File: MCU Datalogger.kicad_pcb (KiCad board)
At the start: 2 copper layers, 29 parts, among them J1 Conn_01x04_Male, J2 Conn_01x09_Male, J3 Conn_01x04_Male, J4 Conn_02x03_Odd_Even, U1 24LC1025, U2 DS1337S+, U3 24LC1025, U4 ATMEGA328-AU, Y1 32.768KHz, Y2 16MHz

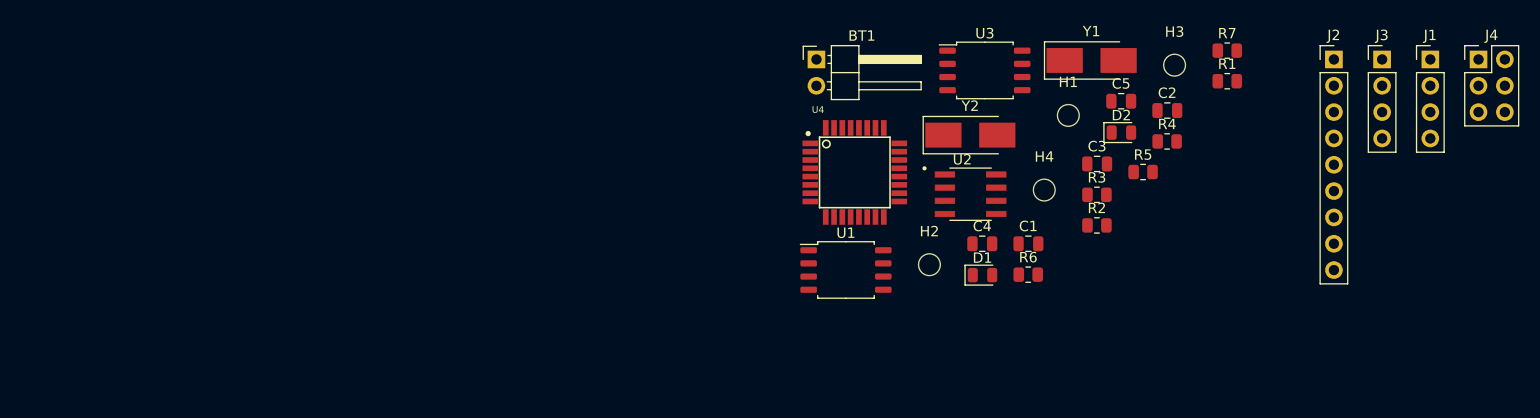
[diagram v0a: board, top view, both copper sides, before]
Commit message: PCB footprint placement
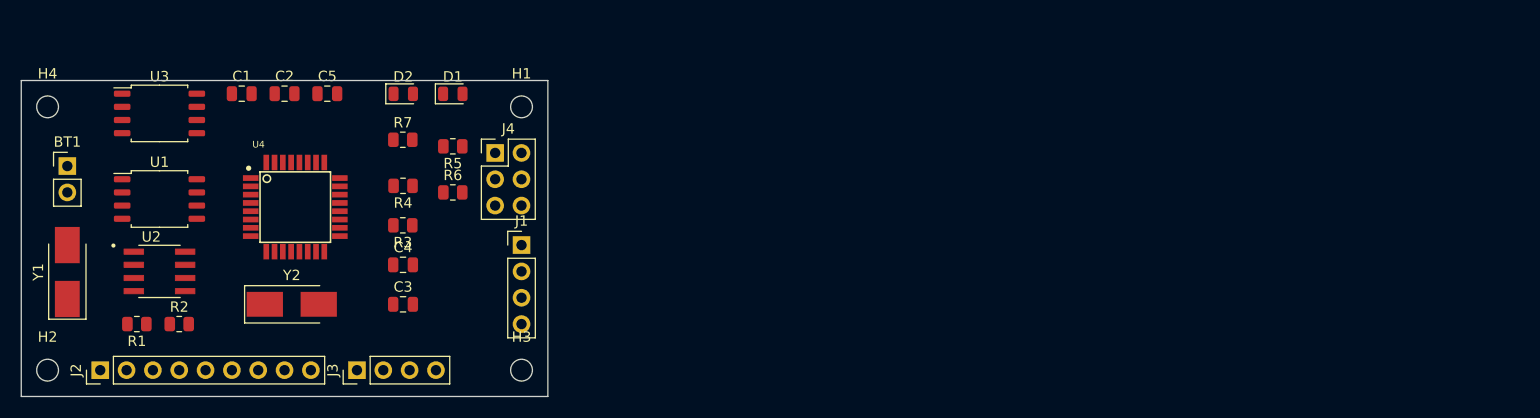
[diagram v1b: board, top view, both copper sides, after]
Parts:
- BT1: footprint Connector_PinHeader_2.54mm:PinHeader_1x02_P2.54mm_Horizontal -> Connector_PinHeader_2.54mm:PinHeader_1x02_P2.54mm_Vertical
- moved J2 122.7 mm to (72.4, 102.9), turned to 90 degrees
- moved R1 107.8 mm to (75.9, 98.4), turned to 180 degrees
- moved J3 103.3 mm to (97.2, 102.9), turned to 90 degrees
- moved Y1 100.9 mm to (69.2, 93.4), turned to 90 degrees
- moved H4 96.5 mm to (67.3, 77.5)
- moved J4 95.3 mm to (110.5, 81.9)
- moved J1 89.5 mm to (113.0, 90.8)
- moved R2 89.0 mm to (80.0, 98.4)
- moved H2 85.7 mm to (67.3, 102.9)
- moved C2 85.2 mm to (90.2, 76.2)
- moved R7 80.0 mm to (101.6, 80.6)
- moved U3 79.7 mm to (78.1, 78.1)
- moved U2 78.6 mm to (78.1, 93.3)
- moved C1 77.3 mm to (86.0, 76.2)
- moved C5 76.6 mm to (94.3, 76.2)
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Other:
- board outline added: 50.8 x 30.5 mm

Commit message: rooting
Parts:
- turned C3 to 180 degrees
- turned C4 to 180 degrees
- turned Y2 to 180 degrees
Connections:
- R3 pad 1: Net-(R3-Pad1) -> /Vcc
- R4 pad 1: Net-(R3-Pad1) -> /Vcc
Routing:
- net GND: track 0.00 -> 153.5 mm, vias 0 -> 7
- net /Vcc: track 0.00 -> 133.3 mm, vias 0 -> 10
- net /SCK: track 0.00 -> 116.5 mm, vias 0 -> 8
- net /SDA: track 0.00 -> 92.8 mm, vias 0 -> 6
- net Net-(U4-Pad18): track 0.00 -> 71.5 mm, vias 0 -> 5
- net Net-(C2-Pad2): track 0.00 -> 38.1 mm, vias 0 -> 2
- net /D2: track 0.00 -> 33.4 mm, vias 0 -> 3
- net /RESET: track 0.00 -> 29.5 mm, vias 0 -> 3
- net /D3: track 0.00 -> 27.0 mm, vias 0 -> 1
- net /TX: track 0.00 -> 26.5 mm, vias 0 -> 1
- net /D4: track 0.00 -> 26.4 mm, vias 0 -> 4
- net /MOSI: track 0.00 -> 25.9 mm
- net /RX: track 0.00 -> 25.1 mm, vias 0 -> 1
- net /MISO: track 0.00 -> 23.2 mm, vias 0 -> 2
- net Net-(Y2-Pad1): track 0.00 -> 18.3 mm
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
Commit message: silk
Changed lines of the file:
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@@
     (property "Sheetname" "Connectors")
     (attr through_hole)
-    (fp_text reference "J1" (at 0 -2.33) (layer "F.SilkS")
-      (effects (font (size 1 1) (thickness 0.15)))
-    )
-    (fp_text value "Conn_01x04_Male" (at 0 9.95) (layer "F.Fab")
+    (fp_text reference "J1" (at -2.54 8.255) (layer "F.SilkS")
+      (effects (font (size 1 1) (thickness 0.15)))
+    )
+    (fp_text value "Conn_01x04_Male" (at 0 9.95) (layer "F.Fab") hide
       (effects (font (size 1 1) (thickness 0.15)))
     )
@@
       (effects (font (size 1 1) (thickness 0.15)))
     )
-    (fp_text value "Conn_01x09_Male" (at 0 22.65 90) (layer "F.Fab")
-      (effects (font (size 1 1) (thickness 0.15)))
-    )
-    (fp_text user "${REFERENCE}" (at -1.27 10.16) (layer "F.Fab")
+    (fp_text value "Conn_01x09_Male" (at 0 22.65 90) (layer "F.Fab") hide
+      (effects (font (size 1 1) (thickness 0.15)))
+    )
+    (fp_text user "${REFERENCE}" (at -1.27 10.16) (layer "F.Fab") hide
       (effects (font (size 1 1) (thickness 0.15)))
     )
@@
     (property "Sheetname" "")
     (attr exclude_from_pos_files)
-    (fp_text reference "H3" (at 0 -3.2) (layer "F.SilkS")
-      (effects (font (size 1 1) (thickness 0.15)))
-    )
-    (fp_text value "MountingHole" (at 0 3.2) (layer "F.Fab")
-      (effects (font (size 1 1) (thickness 0.15)))
-    )
-    (fp_text user "${REFERENCE}" (at 0.3 0) (layer "F.Fab")
+    (fp_text reference "H3" (at 0 -3.2) (layer "F.SilkS") hide
+      (effects (font (size 1 1) (thickness 0.15)))
+    )
+    (fp_text value "MountingHole" (at 0 3.2) (layer "F.Fab") hide
+      (effects (font (size 1 1) (thickness 0.15)))
+    )
+    (fp_text user "${REFERENCE}" (at 0.3 0) (layer "F.Fab") hide
       (effects (font (size 1 1) (thickness 0.15)))
     )
@@
     (property "Sheetname" "")
     (attr smd)
-    (fp_text reference "D2" (at 0 -1.65) (layer "F.SilkS")
+    (fp_text reference "D2" (at -0.02 1.89) (layer "F.SilkS")
       (effects (font (size 1 1) (thickness 0.15)))
     )
@@
     (property "Sheetname" "Connectors")
     (attr through_hole)
-    (fp_text reference "J4" (at 1.27 -2.33) (layer "F.SilkS")
-      (effects (font (size 1 1) (thickness 0.15)))
-    )
-    (fp_text value "Conn_02x03_Odd_Even" (at 1.27 7.41) (layer "F.Fab")
+    (fp_text reference "J4" (at 0.005 -3.175) (layer "F.SilkS")
+      (effects (font (size 1 1) (thickness 0.15)))
+    )
+    (fp_text value "Conn_02x03_Odd_Even" (at 1.27 7.41) (layer "F.Fab") hide
       (effects (font (size 1 1) (thickness 0.15)))
     )
@@
     (property "Sheetname" "")
     (attr smd)
-    (fp_text reference "C5" (at 0 -1.68) (layer "F.SilkS")
+    (fp_text reference "C5" (at 2.86 0) (layer "F.SilkS")
       (effects (font (size 1 1) (thickness 0.15)))
     )
@@
       (effects (font (size 1 1) (thickness 0.15)))
     )
-    (fp_text value "Conn_01x04_Male" (at 0 9.95 90) (layer "F.Fab")
+    (fp_text value "Conn_01x04_Male" (at 0 9.95 90) (layer "F.Fab") hide
       (effects (font (size 1 1) (thickness 0.15)))
     )
@@
     (property "Sheetname" "")
     (attr smd)
-    (fp_text reference "D1" (at 0 -1.65) (layer "F.SilkS")
+    (fp_text reference "D1" (at 0.2775 1.89) (layer "F.SilkS")
       (effects (font (size 1 1) (thickness 0.15)))
     )
@@
       (effects (font (size 1 1) (thickness 0.15)))
     )
-    (fp_text value "MountingHole" (at 0 3.2) (layer "F.Fab")
-      (effects (font (size 1 1) (thickness 0.15)))
-    )
-    (fp_text user "${REFERENCE}" (at 0.3 0) (layer "F.Fab")
+    (fp_text value "MountingHole" (at 0 3.2) (layer "F.Fab") hide
+      (effects (font (size 1 1) (thickness 0.15)))
+    )
+    (fp_text user "${REFERENCE}" (at 0.3 0) (layer "F.Fab") hide
       (effects (font (size 1 1) (thickness 0.15)))
     )
@@
     (property "Sheetname" "")
     (attr exclude_from_pos_files)
-    (fp_text reference "H1" (at 0 -3.2) (layer "F.SilkS")
-      (effects (font (size 1 1) (thickness 0.15)))
-    )
-    (fp_text value "MountingHole" (at 0 3.2) (layer "F.Fab")
+    (fp_text reference "H1" (at 0 -3.2) (layer "F.SilkS") hide
+      (effects (font (size 1 1) (thickness 0.15)))
+    )
+    (fp_text value "MountingHole" (at 0 3.2) (layer "F.Fab") hide
       (effects (font (size 1 1) (thickness 0.15)))
     )
@@
     (property "Sheetname" "")
     (attr exclude_from_pos_files)
-    (fp_text reference "H4" (at 0 -3.2) (layer "F.SilkS")
-      (effects (font (size 1 1) (thickness 0.15)))
-    )
-    (fp_text value "MountingHole" (at 0 3.2) (layer "F.Fab")
-      (effects (font (size 1 1) (thickness 0.15)))
-    )
-    (fp_text user "${REFERENCE}" (at 0.3 0) (layer "F.Fab")
+    (fp_text reference "H4" (at 0 -3.2) (layer "F.SilkS") hide
+      (effects (font (size 1 1) (thickness 0.15)))
+    )
+    (fp_text value "MountingHole" (at 0 3.2) (layer "F.Fab") hide
+      (effects (font (size 1 1) (thickness 0.15)))
+    )
+    (fp_text user "${REFERENCE}" (at 0.3 0) (layer "F.Fab") hide
       (effects (font (size 1 1) (thickness 0.15)))
     )
@@
     (property "Sheetname" "")
     (attr smd)
-    (fp_text reference "C2" (at 0 -1.68) (layer "F.SilkS")
+    (fp_text reference "C2" (at 0.261252 1.905) (layer "F.SilkS")
       (effects (font (size 1 1) (thickness 0.15)))
     )
@@
     (property "Sheetname" "")
     (attr smd)
-    (fp_text reference "U3" (at 0 -3.56) (layer "F.SilkS")
+    (fp_text reference "U3" (at 0 3.81) (layer "F.SilkS")
       (effects (font (size 1 1) (thickness 0.15)))
     )
@@
     (property "Sheetname" "")
     (attr smd)
-    (fp_text reference "C1" (at 0 -1.68) (layer "F.SilkS")
+    (fp_text reference "C1" (at 0.261252 1.905) (layer "F.SilkS")
       (effects (font (size 1 1) (thickness 0.15)))
     )
@@
   (segment (start 72.51 92.71) (end 75.63 92.71) (width 0.25) (layer "F.Cu") (net 26))
   (segment (start 69.215 96.005) (end 72.51 92.71) (width 0.25) (layer "F.Cu") (net 26))
+  (zone (net 0) (net_name "") (layer "F.Cu") (hatch edge 0.508)
+    (connect_pads (clearance 0))
+    (min_thickness 0.254)
+    (keepout (tracks not_allowed) (vias not_allowed) (pads not_allowed ) (copperpour allowed) (footprints allowed))
+    (fill (thermal_gap 0.508) (thermal_bridge_width 0.508))
+    (polygon
+      (pts
+        (xy 120.015 107.315)
+        (xy 62.865 108.585)
+        (xy 61.595 73.66)
+        (xy 120.015 73.025)
+      )
+    )
+  )
+  (zone (net 0) (net_name "") (layer "B.Cu") (hatch edge 0.508)
+    (connect_pads (clearance 0))
+    (min_thickness 0.254)
+    (keepout (tracks not_allowed) (vias not_allowed) (pads not_allowed ) (copperpour allowed) (footprints allowed))
+    (fill (thermal_gap 0.508) (thermal_bridge_width 0.508))
+    (polygon
+      (pts
+        (xy 118.11 106.045)
+        (xy 63.5 107.95)
+        (xy 62.865 74.295)
+        (xy 117.475 73.66)
+      )
+    )
+  )
 )

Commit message: 4layer
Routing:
- net GND: track 153.5 -> 0.00 mm, vias 7 -> 0
- net /Vcc: track 133.3 -> 0.00 mm, vias 10 -> 0
- net /SCK: track 116.5 -> 0.00 mm, vias 8 -> 0
- net /SDA: track 92.8 -> 0.00 mm, vias 6 -> 0
- net Net-(U4-Pad18): track 71.5 -> 0.00 mm, vias 5 -> 0
- net Net-(C2-Pad2): track 38.1 -> 0.00 mm, vias 2 -> 0
- net /D2: track 33.4 -> 0.00 mm, vias 3 -> 0
- net /RESET: track 29.5 -> 0.00 mm, vias 3 -> 0
- net /D3: track 27.0 -> 0.00 mm, vias 1 -> 0
- net /TX: track 26.5 -> 0.00 mm, vias 1 -> 0
- net /D4: track 26.4 -> 0.00 mm, vias 4 -> 0
- net /MOSI: track 25.9 -> 0.00 mm
- net /RX: track 25.1 -> 0.00 mm, vias 1 -> 0
- net /MISO: track 23.2 -> 0.00 mm, vias 2 -> 0
- net Net-(Y2-Pad1): track 18.3 -> 0.00 mm
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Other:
- copper layers 2 -> 4

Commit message: router
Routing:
- net GND: track 0.00 -> 165.1 mm, vias 0 -> 1
- net /Vcc: track 0.00 -> 133.3 mm
- net /SCK: track 0.00 -> 98.3 mm, vias 0 -> 3
- net /SDA: track 0.00 -> 61.8 mm
- net Net-(U4-Pad18): track 0.00 -> 51.3 mm, vias 0 -> 3
- net /TX: track 0.00 -> 30.1 mm, vias 0 -> 1
- net /D2: track 0.00 -> 26.8 mm, vias 0 -> 1
- net /D3: track 0.00 -> 26.2 mm
- net /RESET: track 0.00 -> 26.0 mm, vias 0 -> 1
- net /RX: track 0.00 -> 25.1 mm, vias 0 -> 1
- net Net-(C2-Pad2): track 0.00 -> 24.1 mm, vias 0 -> 3
- net /MOSI: track 0.00 -> 23.8 mm, vias 0 -> 1
- net /D4: track 0.00 -> 23.3 mm
- net /MISO: track 0.00 -> 20.4 mm, vias 0 -> 1
- net Net-(Y2-Pad1): track 0.00 -> 18.0 mm, vias 0 -> 2
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
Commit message: error
git commit -amerror
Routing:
- net /SDA: track 61.8 -> 100.9 mm
- net /SCK: track 98.3 -> 137.3 mm, vias 3 -> 1
- net /Vcc: track 133.3 -> 148.5 mm
- net /RESET: track 26.0 -> 31.2 mm
- net Net-(U4-Pad18): track 51.3 -> 55.2 mm
- net /TX: track 30.1 -> 26.7 mm
- net Net-(U4-Pad20): track 7.93 -> 11.2 mm
- net /MOSI: track 23.8 -> 27.0 mm
- net /D3: track 26.2 -> 24.2 mm, vias 0 -> 1
- net Net-(C2-Pad2): track 24.1 -> 26.0 mm, vias 3 -> 0
- net GND: track 165.1 -> 163.5 mm, vias 1 -> 2
- net /D2: track 26.8 -> 28.0 mm
- net /D7: track 14.4 -> 13.5 mm, vias 0 -> 1
- net /MISO: track 20.4 -> 21.2 mm
- net /D4: track 23.3 -> 23.8 mm, vias 0 -> 1
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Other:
- copper layers 4 -> 2

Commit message: routing
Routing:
- net /SCK: track 137.3 -> 94.6 mm, vias 1 -> 0
- net /SDA: track 100.9 -> 68.5 mm, vias 0 -> 2
- net /Vcc: track 148.5 -> 122.0 mm, vias 0 -> 1
- net GND: track 163.5 -> 152.3 mm
- net /RESET: track 31.2 -> 25.7 mm
- net Net-(U4-Pad20): track 11.2 -> 7.93 mm
- net Net-(C2-Pad2): track 26.0 -> 23.6 mm, vias 0 -> 3
- net Net-(U4-Pad18): track 55.2 -> 52.8 mm
- net /MOSI: track 27.0 -> 25.4 mm
- net /TX: track 26.7 -> 27.7 mm
- net /D7: track 13.5 -> 14.4 mm, vias 1 -> 0
- net /MISO: track 21.2 -> 20.4 mm
- net /D6: track 14.2 -> 14.4 mm, vias 1 -> 0
- net /D5: track 14.9 -> 15.1 mm, vias 1 -> 0
- net Net-(Y2-Pad1): track 18.3 -> 18.5 mm, vias 0 -> 2
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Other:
- copper layers 2 -> 4
